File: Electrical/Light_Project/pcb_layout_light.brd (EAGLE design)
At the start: 160 x 100 mm, 6 parts, among them U1 REG710NA-3.3/3K, U2 ATTINY85V-10SU

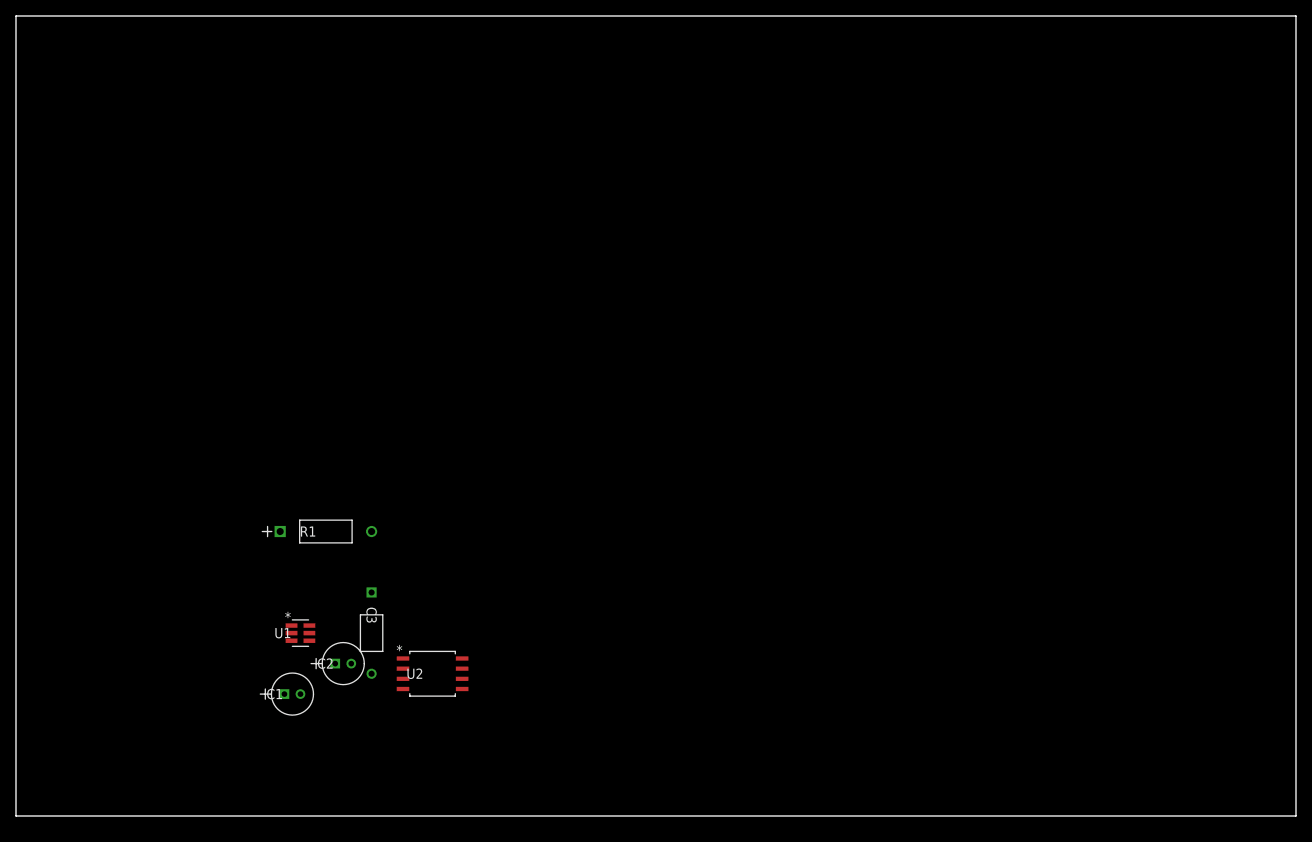
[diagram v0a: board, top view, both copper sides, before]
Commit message: Route PCB (not optimized)
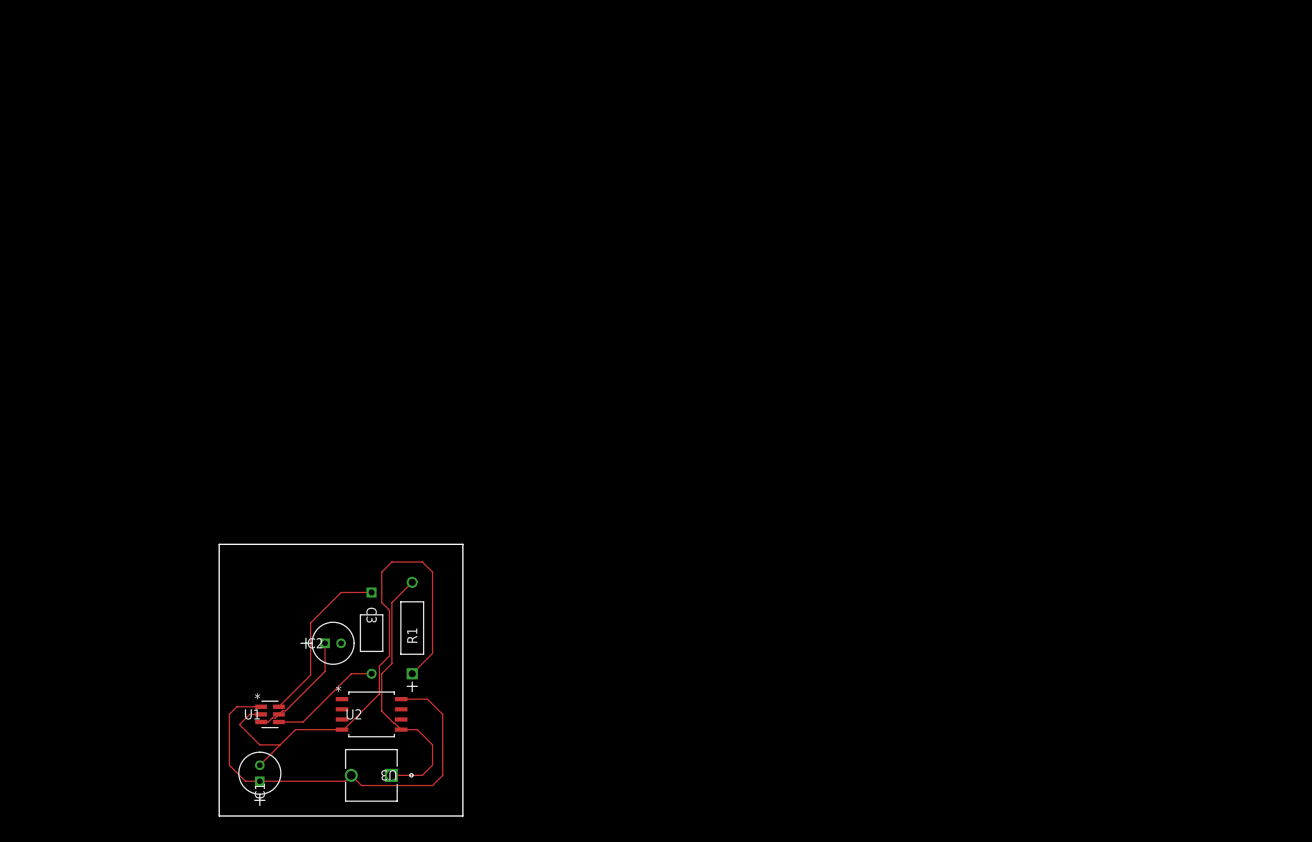
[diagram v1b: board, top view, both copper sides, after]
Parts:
- added U3: FSM8JRT, button:SWITCH_FSM4JRT
- moved U1 10.9 mm to (31.8, 12.7)
- moved C1 10.2 mm to (30.5, 6.35), turned to 90 degrees
- moved U2 9.16 mm to (44.5, 12.7)
- moved R1 8.13 mm to (49.5, 29.2), turned to 90 degrees
- moved C2 2.84 mm to (40.6, 21.6)
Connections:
- net N$1: now also U3.2
- net N$4: now also U1.3
- net N$5: now also U3.1
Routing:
- net GND: track 0.00 -> 65.3 mm
- net N$1: track 0.00 -> 53.2 mm
- net N$5: track 0.00 -> 34.0 mm
- net N$2: track 0.00 -> 21.3 mm
- net N$4: track 0.00 -> 14.1 mm
- net N$3: track 0.00 -> 14.1 mm
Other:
- board size 160 x 100 mm -> 30.5 x 34 mm

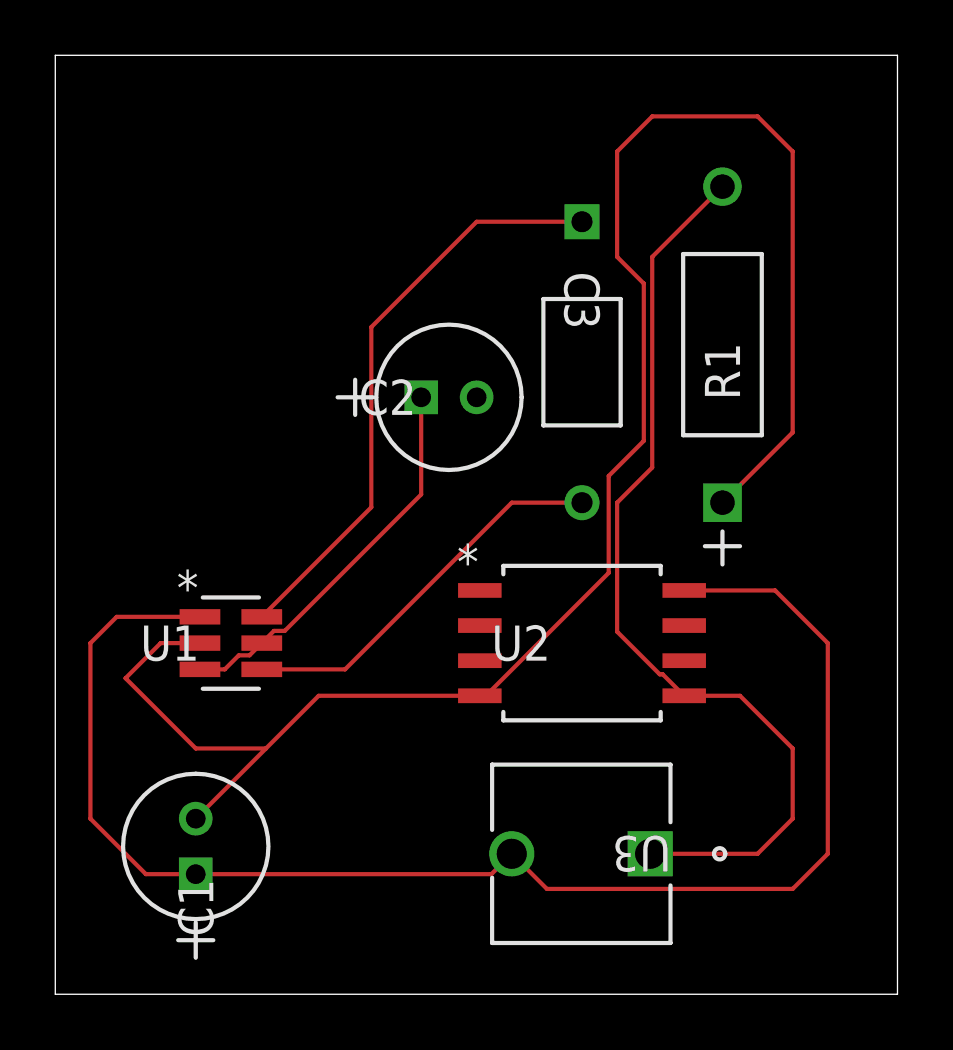
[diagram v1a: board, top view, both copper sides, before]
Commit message: use surface mount resistor in diagram
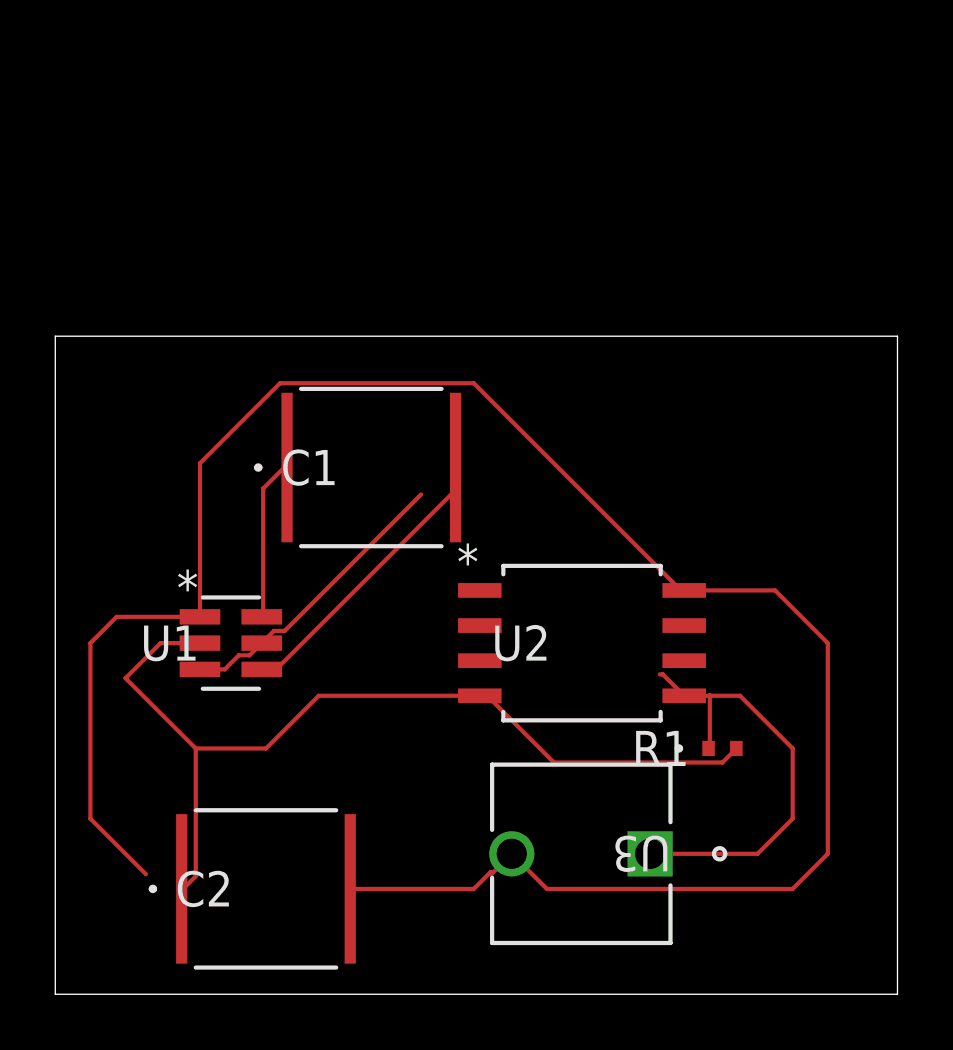
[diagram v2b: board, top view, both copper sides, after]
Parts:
- removed C3: C410C224M5U5TA7200, 22ufcap:CAP_C410
- C1, C2: value UPS1H2R2MDD1TD -> C5750X7T2E225K250KE; device 2.2ufCap:U1-E -> 2p2SFcap:CAP_5750
- R1: value CF14JT10K0 -> RR0510P-103-D; device 10k Resistor:STA_CF14 -> 10kresistor:RES_0510
- moved R1 20.3 mm to (49.5, 8.89), turned to 0 degrees
- moved C2 19.3 mm to (33.0, 3.81)
- moved C1 14.2 mm to (36.8, 19.1), turned to 0 degrees
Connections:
- removed net VCC: C2.2
- net GND: now also C2.1, R1.2; no longer C1.2, R1.1
- net N$1: now also C2.2; no longer C1.1
- net N$2: now also C1.1; no longer C3.1
- net N$3: now also C1.2; no longer C3.2
- net N$4: no longer C2.1
- net N$5: now also R1.1; no longer R1.2
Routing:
- net GND: track 65.3 -> 33.9 mm
- net N$1: track 53.2 -> 73.4 mm
- net N$5: track 34.0 -> 16.1 mm
- net N$2: track 21.3 -> 5.83 mm
- net N$4: track 14.1 -> 10.6 mm
- net N$3: track 14.1 -> 10.6 mm
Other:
- board size 30.5 x 34 mm -> 30.5 x 23.8 mm

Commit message: add pdf of new layout
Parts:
- moved C1 16.5 mm to (30.5, 3.81), turned to 180 degrees
- moved C2 13.0 mm to (30.5, 16.5)
- moved U2 5.24 mm to (39.4, 11.4)
- moved R1 4.02 mm to (45.7, 7.62), turned to 270 degrees
- moved U3 4.02 mm to (38.1, 3.81)
- moved U1 2.84 mm to (30.5, 10.2), turned to 270 degrees
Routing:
- net N$1: track 73.4 -> 40.6 mm
- net GND: track 33.9 -> 24.6 mm
- net N$4: track 10.6 -> 2.63 mm
- net N$5: track 16.1 -> 10.5 mm
- net N$3: track 10.6 -> 6.10 mm
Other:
- board size 30.5 x 23.8 mm -> 24.1 x 21.3 mm

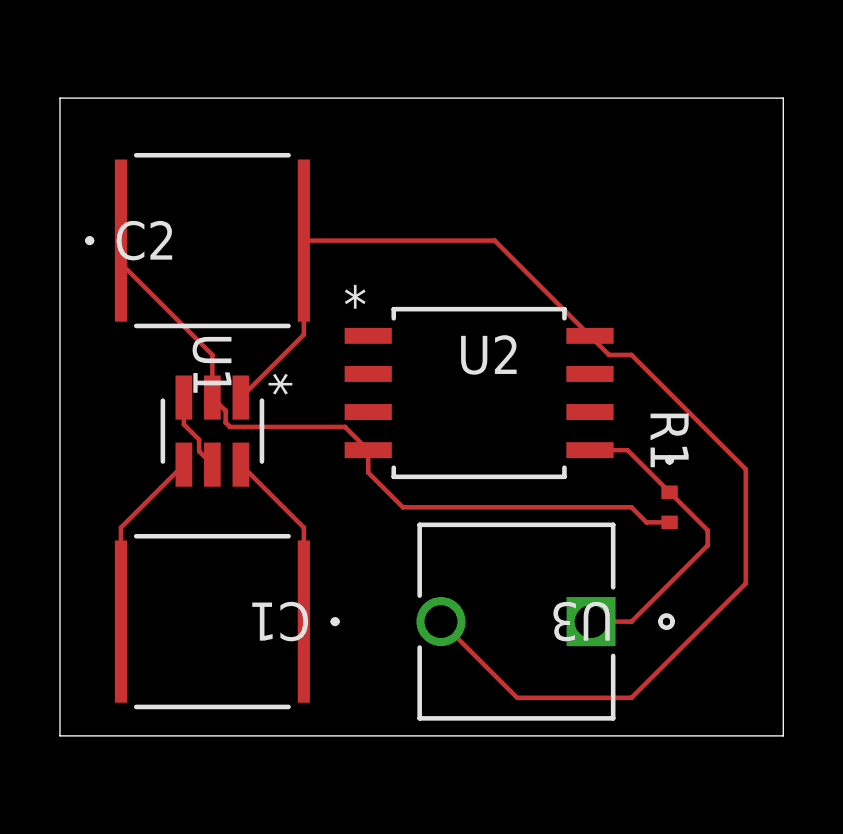
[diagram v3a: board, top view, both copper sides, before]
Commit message: add holes on pcb
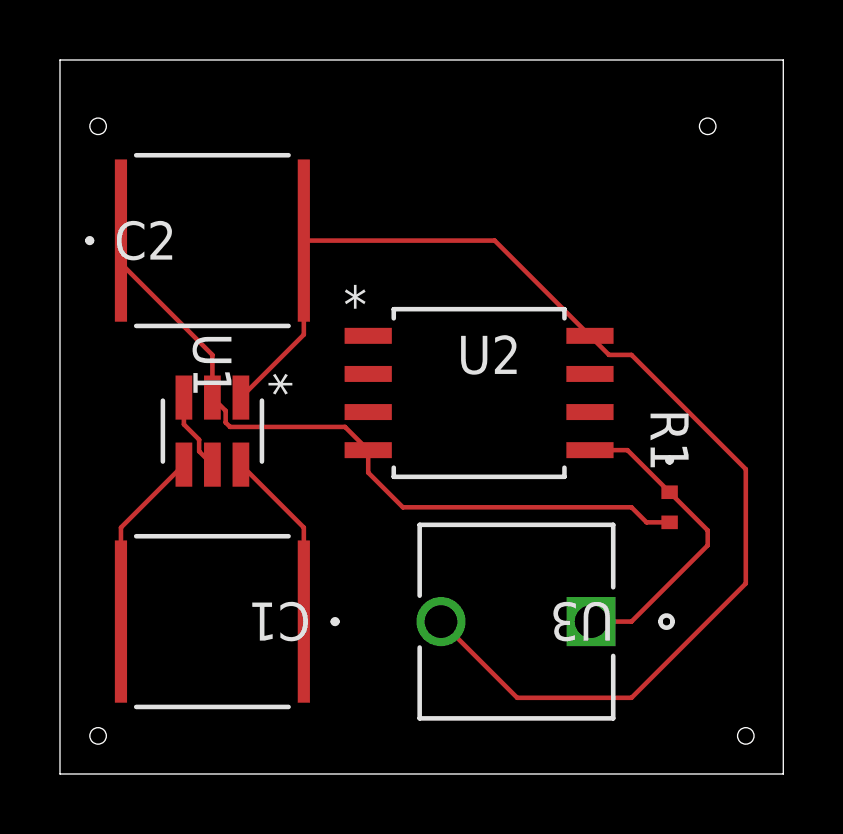
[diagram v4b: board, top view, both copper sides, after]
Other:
- board size 24.1 x 21.3 mm -> 24.1 x 23.8 mm
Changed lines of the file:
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@@
 <layer number="43" name="vRestrict" color="2" fill="10" visible="yes" active="yes"/>
 <layer number="44" name="Drills" color="7" fill="1" visible="no" active="yes"/>
-<layer number="45" name="Holes" color="7" fill="1" visible="no" active="yes"/>
+<layer number="45" name="Holes" color="7" fill="1" visible="yes" active="yes"/>
 <layer number="46" name="Milling" color="3" fill="1" visible="no" active="yes"/>
 <layer number="47" name="Measures" color="7" fill="1" visible="no" active="yes"/>
@@
 <board>
 <plain>
-<wire x1="25.4" y1="0" x2="49.51" y2="0" width="0" layer="20"/>
-<wire x1="49.51" y1="0" x2="49.51" y2="21.26" width="0" layer="20"/>
-<wire x1="49.51" y1="21.26" x2="25.4" y2="21.26" width="0" layer="20"/>
-<wire x1="25.4" y1="21.26" x2="25.4" y2="0" width="0" layer="20"/>
+<wire x1="25.4" y1="-1.27" x2="49.51" y2="-1.27" width="0" layer="20"/>
+<wire x1="49.51" y1="-1.27" x2="49.51" y2="22.53" width="0" layer="20"/>
+<wire x1="49.51" y1="22.53" x2="25.4" y2="22.53" width="0" layer="20"/>
+<wire x1="25.4" y1="22.53" x2="25.4" y2="-1.27" width="0" layer="20"/>
+<hole x="46.99" y="20.32" drill="0.55"/>
+<hole x="26.67" y="20.32" drill="0.55"/>
+<hole x="48.26" y="0" drill="0.55"/>
+<hole x="26.67" y="0" drill="0.55"/>
 </plain>
 <attributes>

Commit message: update PCB layout with LED
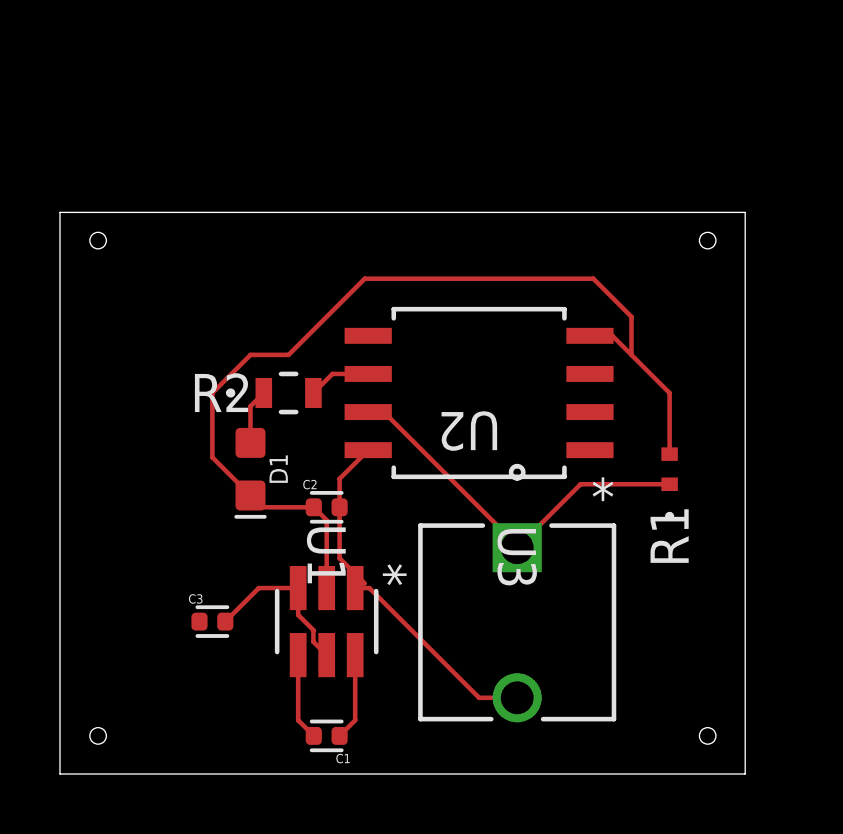
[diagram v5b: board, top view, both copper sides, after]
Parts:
- added C3: GRJ155R60J106ME11D, GRJ155R60J106ME11D:CAPC1005X55N
- added D1: GREEN, SparkFun-LED:LED-0603
- added R2: RR0816P-112-D, 1p1koSF:RES_0816
- C1, C2: value C5750X7T2E225K250KE -> GRJ155R60J106ME11D; device 2p2SFcap:CAP_5750 -> GRJ155R60J106ME11D:CAPC1005X55N
- moved C2 9.67 mm to (34.3, 7.62)
- moved U1 7.41 mm to (34.3, 3.81)
- moved C1 5.39 mm to (34.3, 0.00)
- moved U3 3.59 mm to (40.6, 1.27), turned to 270 degrees
- moved R1 1.27 mm to (45.7, 8.89), turned to 90 degrees
- turned U2 to 180 degrees
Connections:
- new net N$6: D1.A, R2.1
- new net N$7: R2.2, U2.6
- new net VCC: C3.1
- net GND: now also D1.C
- net N$4: now also C3.2
- net N$5: now also U2.7; no longer U2.5
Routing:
- net N$1: track 40.6 -> 12.1 mm
- net GND: track 24.6 -> 31.9 mm
- net N$3: track 6.10 -> 2.91 mm
- net N$2: track 6.10 -> 2.91 mm
- net N$4: track 2.63 -> 5.52 mm
- net N$5: track 10.5 -> 12.8 mm
- net N$7: track 0.00 -> 2.09 mm
- net N$6: track 0.00 -> 1.85 mm
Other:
- board size 24.1 x 23.8 mm -> 22.8 x 18.7 mm
